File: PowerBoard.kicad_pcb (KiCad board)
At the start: 2 copper layers, 138.9 x 105.6 mm, 15 parts, among them J101 Conn_01x04_Pin, J102 Conn_01x04_Pin, J103 Conn_01x04_Pin, J104 Conn_01x04_Pin, J105 Conn_01x02_Pin, J106 Conn_01x02_Pin, J107 Conn_01x02_Pin, J108 Conn_01x06_Pin, J109 Conn_01x06_Pin, J110 USB_C_Receptacle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

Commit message: weedies
weedies
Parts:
- added G***: LOGO, memes:weedies2, F.Cu at (130.0, 82.4)
- moved U101 50.8 mm to (115.9, 129.7)
- moved J102 46.9 mm to (131.4, 52.1)
- moved J101 46.9 mm to (114.8, 52.0)
- moved J103 46.9 mm to (148.4, 52.4)
- moved J104 46.4 mm to (165.2, 52.3)
- moved J109 46.1 mm to (208.1, 48.8)
- moved J106 46.1 mm to (228.3, 48.5)
- moved J105 45.9 mm to (198.0, 48.8)
- moved J108 45.8 mm to (177.9, 48.6)
- moved J110 40.5 mm to (135.3, 134.5), turned to -90 degrees
- moved R104 38.8 mm to (186.3, 76.0)
- moved D101 38.8 mm to (186.4, 73.5)
- moved U103 38.8 mm to (187.2, 63.4)
- moved U104 38.4 mm to (144.5, 112.2)
- moved J107 36.9 mm to (172.1, 95.7)
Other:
- board size 138.9 x 105.6 mm -> 139.1 x 147.4 mm

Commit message: Big Moves
Big Moves
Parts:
- removed G***: LOGO, memes:weedies2
- U101: footprint MCU_Teensy:Teensy_4.1 -> MCU_Teensy:Teensy41_bare_pins
- moved J107 45.4 mm to (209.4, 69.8), turned to 45 degrees
- moved U104 31.5 mm to (172.2, 97.2), turned to 45 degrees
- moved J110 27.6 mm to (118.5, 156.4), turned to 45 degrees
- moved U101 20.7 mm to (114.5, 109.1)
- moved D101 11.7 mm to (183.8, 84.8), turned to 90 degrees
- moved R104 5.92 mm to (183.8, 81.3), turned to -90 degrees
- moved U103 5.52 mm to (187.3, 68.9), turned to 45 degrees
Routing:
- net 3V3: track 0.00 -> 208.3 mm, vias 0 -> 6
- net 5V: track 0.00 -> 159.8 mm, vias 0 -> 2
- net /L298N2_ENA: track 0.00 -> 150.4 mm, vias 0 -> 1
- net /L298N2_IN1: track 0.00 -> 147.2 mm, vias 0 -> 1
- net /L298N2_IN2: track 0.00 -> 142.9 mm, vias 0 -> 1
- net /L298N1_ENA: track 0.00 -> 142.6 mm, vias 0 -> 2
- net /L298N2_IN3: track 0.00 -> 138.4 mm, vias 0 -> 1
- net /L298N1_IN1: track 0.00 -> 137.9 mm, vias 0 -> 2
- net /L298N2_IN4: track 0.00 -> 133.6 mm, vias 0 -> 1
- net /L298N1_IN2: track 0.00 -> 133.1 mm, vias 0 -> 2
- net /L298N2_ENB: track 0.00 -> 129.2 mm, vias 0 -> 1
- net /L298N1_IN3: track 0.00 -> 128.2 mm, vias 0 -> 2
- net /Motor4_A: track 0.00 -> 124.6 mm, vias 0 -> 4
- net /L298N1_IN4: track 0.00 -> 124.5 mm, vias 0 -> 2
- net /Motor4_B: track 0.00 -> 124.4 mm, vias 0 -> 4
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- added copper zone on B.Cu, net GND
- added copper zone on F.Cu, net GND

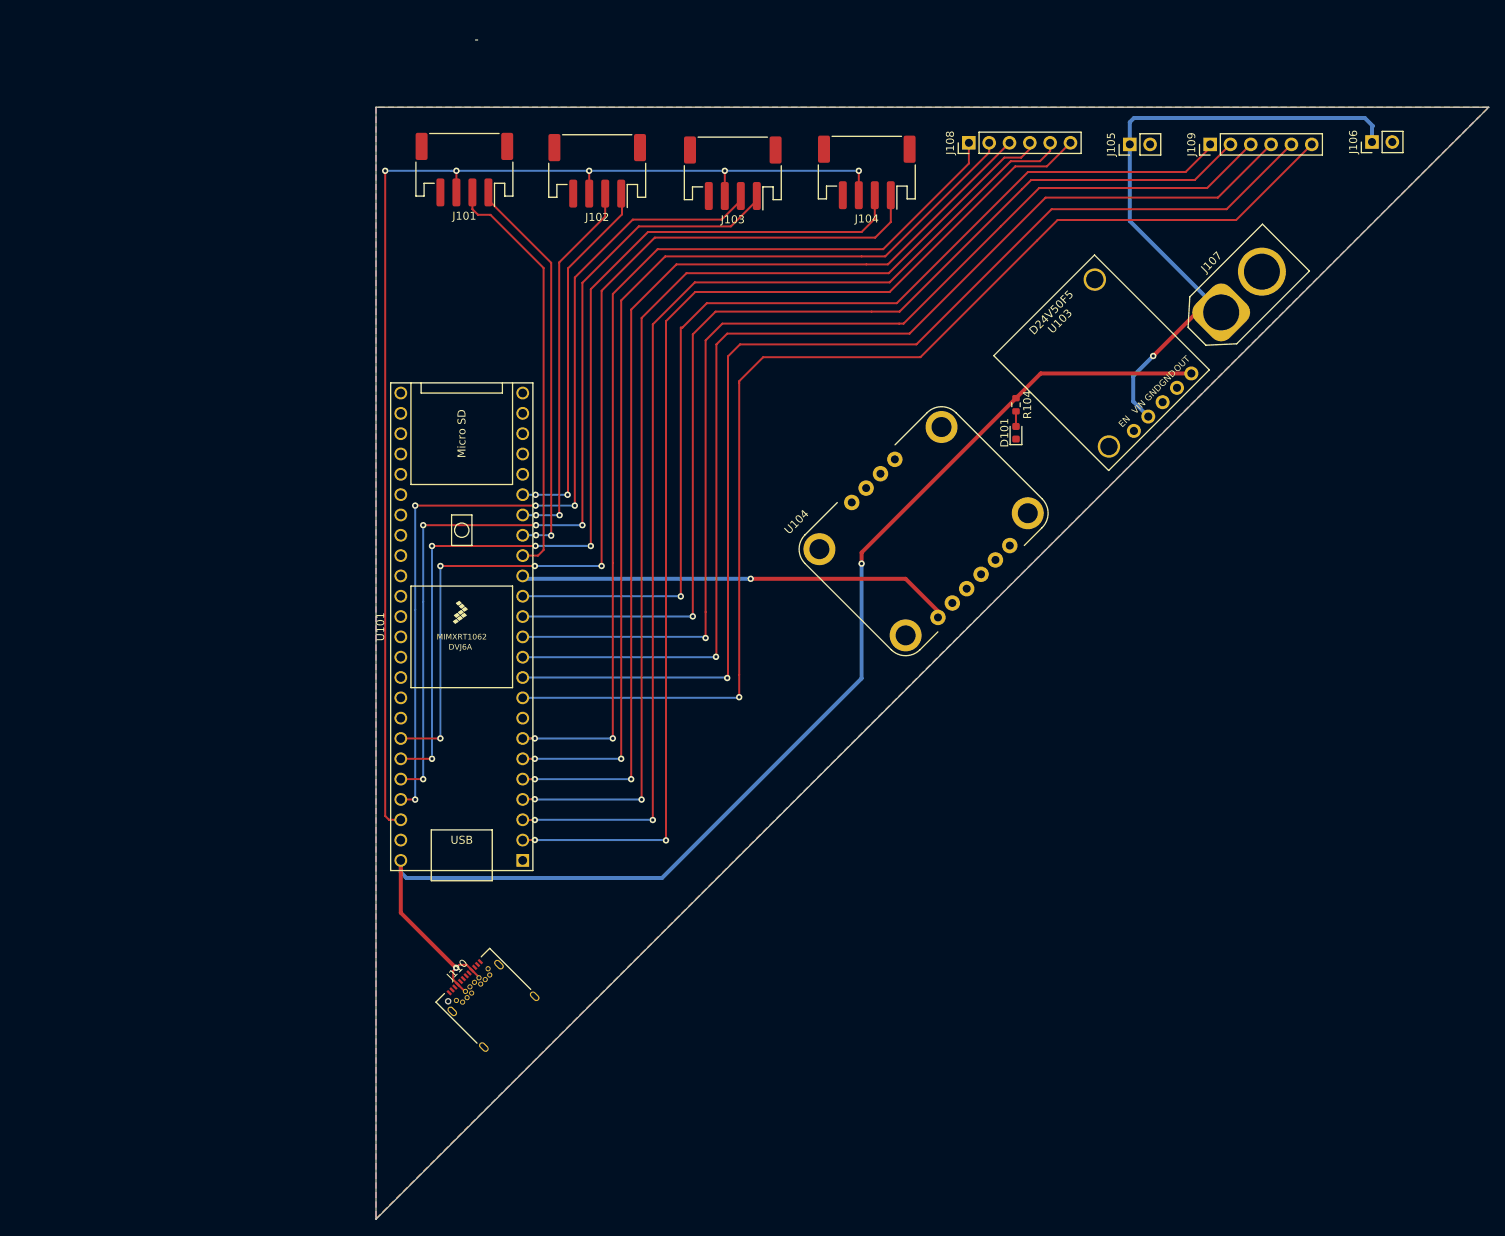
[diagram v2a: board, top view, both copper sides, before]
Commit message: some small routing touchups
made power traces much larger, made battery connector GND pad thermal reliefs larger, organized trace spacing a bit more, deleted some vias that didn't add anything, added a 15mil keepout around the board perimeter for manufacturing, and squared off the 45 degree corners for manufacturing to fix the board edge
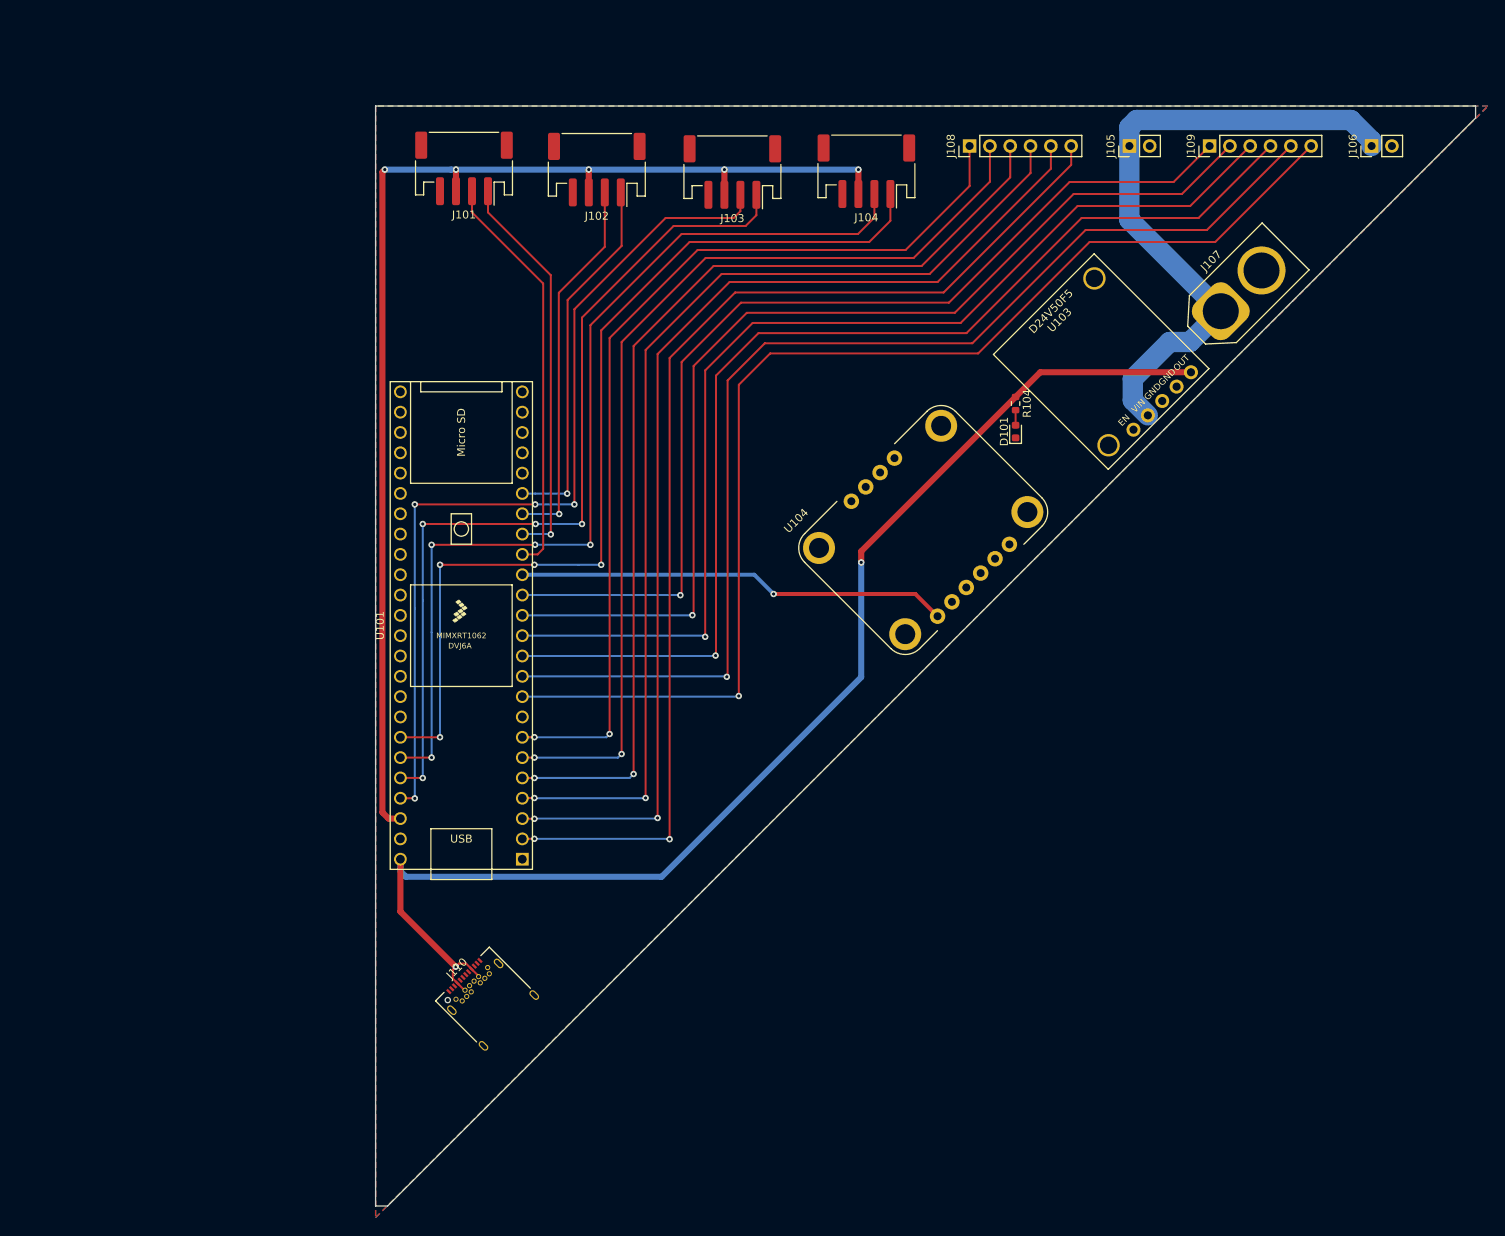
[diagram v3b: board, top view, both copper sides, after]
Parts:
- moved J106 0.50 mm to (228.2, 49.0)
- moved J108 0.41 mm to (178.0, 49.0)
- moved J109 0.21 mm to (208.0, 49.0)
- moved J105 0.21 mm to (198.0, 49.0)
- moved D101 0.16 mm to (183.7, 84.7)
- moved R104 0.16 mm to (183.7, 81.2)
- moved U103 0.16 mm to (187.3, 68.8)
- moved U104 0.16 mm to (172.2, 97.0)
- moved J101 0.16 mm to (114.8, 51.8)
- moved U101 0.16 mm to (114.5, 108.9)
- moved J103 0.16 mm to (148.3, 52.2)
- moved J104 0.16 mm to (165.1, 52.1)
- moved J102 0.16 mm to (131.4, 52.0)
- moved J107 0.16 mm to (209.4, 69.7)
- moved J110 0.16 mm to (118.4, 156.3)
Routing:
- net /L298N2_ENB: track 129.2 -> 126.2 mm
- net /Motor4_B: track 124.4 -> 121.4 mm
- net /Motor4_A: track 124.6 -> 121.8 mm
- net /L298N2_IN4: track 133.6 -> 130.9 mm
- net /L298N2_IN2: track 142.9 -> 140.4 mm
- net /L298N2_IN3: track 138.4 -> 136.0 mm
- net /L298N1_ENB: track 122.2 -> 120.0 mm
- net /L298N2_IN1: track 147.2 -> 145.2 mm
- net VIN: track 81.7 -> 80.0 mm, vias 1 -> 0
- net /L298N1_IN4: track 124.5 -> 122.9 mm
- net /Motor3_A: track 112.3 -> 110.8 mm
- net /L298N1_ENA: track 142.6 -> 141.1 mm
- net /Motor3_B: track 111.4 -> 109.9 mm
- net /L298N1_IN1: track 137.9 -> 136.6 mm
- net /L298N1_IN2: track 133.1 -> 132.1 mm
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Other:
- board size 139.1 x 147.4 mm -> 137.5 x 137.5 mm

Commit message: ready for review
Flipped encoder connector pinout, added mounting holes, fixed battery connector footprint, moved USB C connector, added memes, added placeholder names
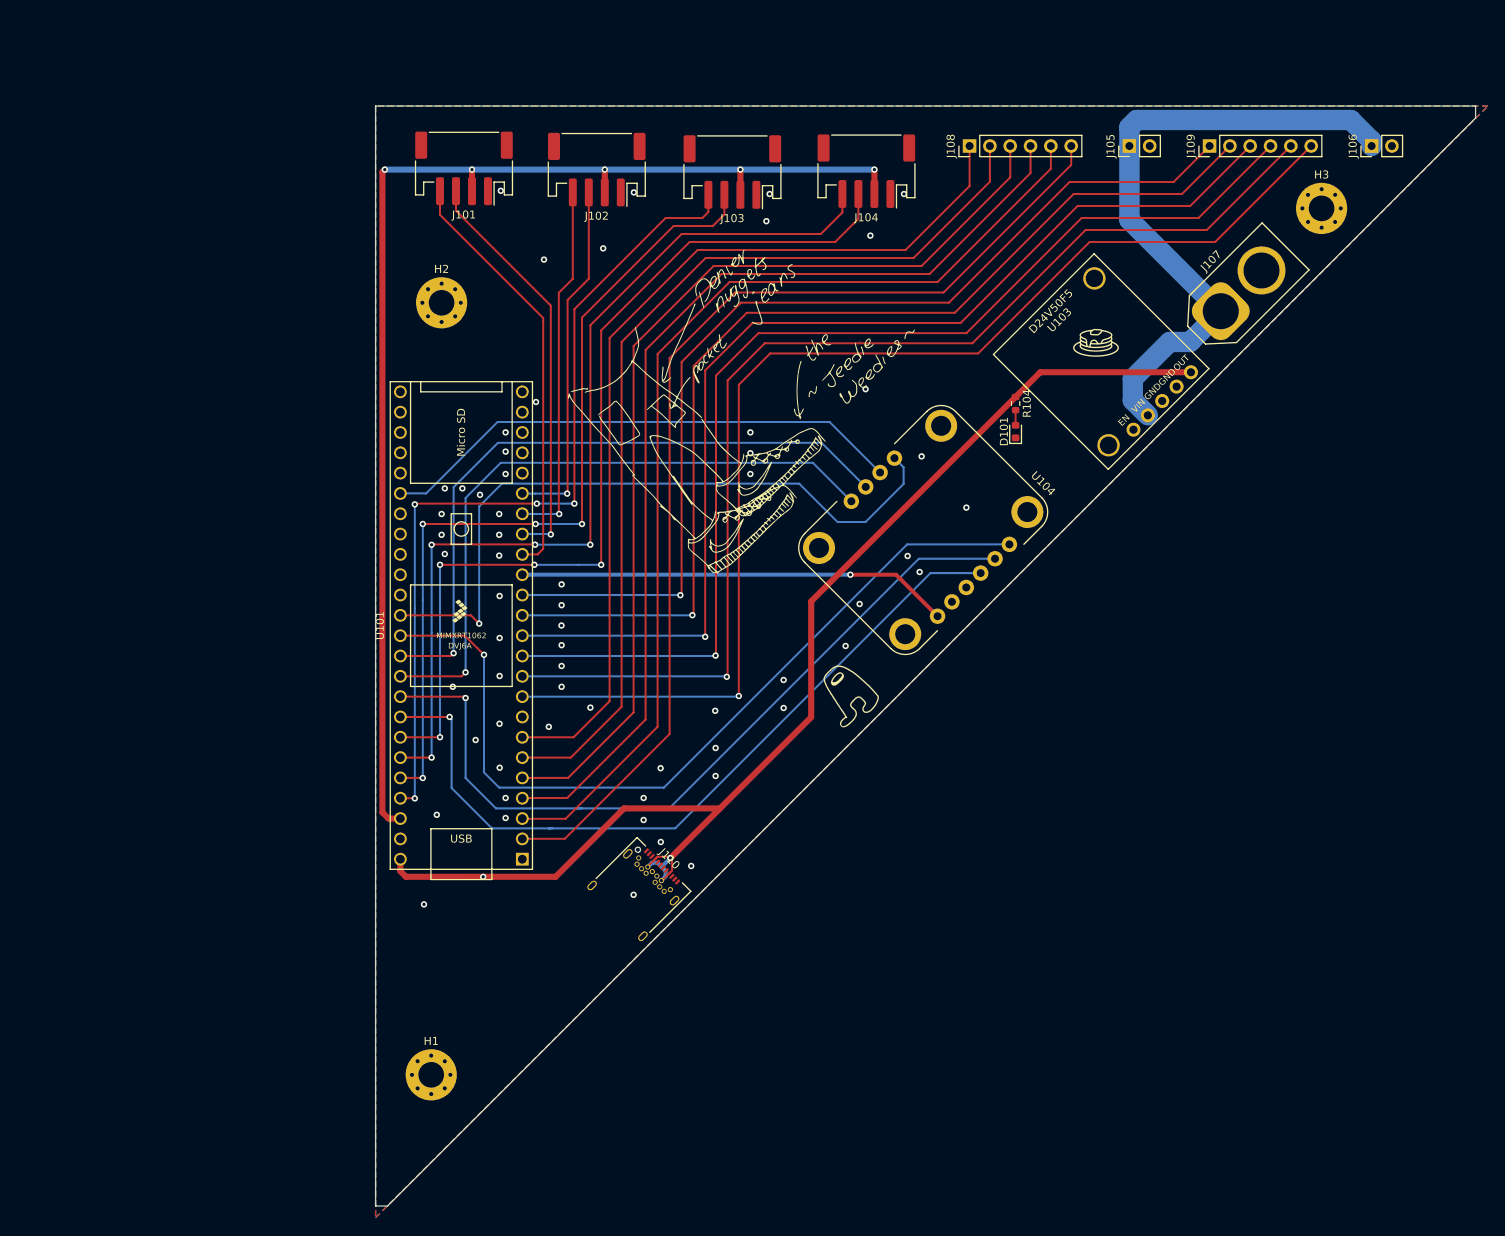
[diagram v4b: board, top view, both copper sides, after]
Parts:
- added G***: LOGO, memes:weedies2, F.Cu at (152.3, 78.0)
- added G***: LOGO, memes:pancakes, F.Cu at (193.8, 73.6)
- added G***: LOGO, memes:Amogus, F.Cu at (162.4, 117.7)
- added H1: MountingHole_Pad, MountingHole:MountingHole_3.2mm_M3_Pad_Via, F.Cu at (110.7, 165.1)
- added H2: MountingHole_Pad, MountingHole:MountingHole_3.2mm_M3_Pad_Via, F.Cu at (112.0, 68.6)
- added H3: MountingHole_Pad, MountingHole:MountingHole_3.2mm_M3_Pad_Via, F.Cu at (222.0, 56.8)
- J107: footprint Connector_AMASS:AMASS_XT60-F_1x02_P7.20mm_Vertical -> Connector_AMASS:AMASS_XT60-M_1x02_P7.20mm_Vertical
- moved J110 22.3 mm to (136.0, 142.6), turned to -45 degrees
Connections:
- J101 pad 1: /Motor1_B -> GND
- J101 pad 2: /Motor1_A -> 3V3
- J101 pad 3: 3V3 -> /Motor1_A
- J101 pad 4: GND -> /Motor1_B
- J102 pad 1: /Motor2_B -> GND
- J102 pad 2: /Motor2_A -> 3V3
- J102 pad 3: 3V3 -> /Motor2_A
- J102 pad 4: GND -> /Motor2_B
- J103 pad 1: /Motor3_B -> GND
- J103 pad 2: /Motor3_A -> 3V3
- J103 pad 3: 3V3 -> /Motor3_A
- J103 pad 4: GND -> /Motor3_B
- J104 pad 1: /Motor4_B -> GND
- J104 pad 2: /Motor4_A -> 3V3
- J104 pad 3: 3V3 -> /Motor4_A
- J104 pad 4: GND -> /Motor4_B
- U101 pad 16: /Motor1_A -> /Motor1_B
- U101 pad 17: /Motor1_B -> /Motor1_A
- U101 pad 18: /Motor2_A -> /Motor2_B
- U101 pad 19: /Motor2_B -> /Motor2_A
- U101 pad 36: unconnected-(U101-14_A0_TX3_SPDIF_OUT-Pad36) -> /IMU_ADR
- U101 pad 37: unconnected-(U101-15_A1_RX3_SPDIF_IN-Pad37) -> /IMU_RST
- U101 pad 38: unconnected-(U101-16_A2_RX4_SCL1-Pad38) -> /IMU_PS1
- U101 pad 39: unconnected-(U101-17_A3_TX4_SDA1-Pad39) -> /IMU_PS0
- U101 pad 40: unconnected-(U101-18_A4_SDA-Pad40) -> /IMU_SCL
- U101 pad 41: unconnected-(U101-19_A5_SCL-Pad41) -> /IMU_SDA
- U101 pad 42: /Motor4_B -> /Motor4_A
- U101 pad 43: /Motor4_A -> /Motor4_B
- U101 pad 44: /Motor3_B -> /Motor3_A
- U101 pad 45: /Motor3_A -> /Motor3_B
- U104 pad 10: unconnected-(U104-PS0-Pad10) -> /IMU_PS0
- U104 pad 4: unconnected-(U104-SDA-Pad4) -> /IMU_SDA
- U104 pad 5: unconnected-(U104-SCL-Pad5) -> /IMU_SCL
- U104 pad 6: unconnected-(U104-RST-Pad6) -> /IMU_RST
- U104 pad 7: unconnected-(U104-ADR-Pad7) -> /IMU_ADR
- U104 pad 9: unconnected-(U104-PS1-Pad9) -> /IMU_PS1
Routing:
- net /IMU_RST: track 0.00 -> 105.2 mm, vias 0 -> 1
- net /IMU_SCL: track 0.00 -> 99.7 mm, vias 0 -> 1
- net /IMU_SDA: track 0.00 -> 97.1 mm, vias 0 -> 1
- net /IMU_ADR: track 0.00 -> 86.8 mm, vias 0 -> 1
- net /IMU_PS1: track 0.00 -> 83.6 mm, vias 0 -> 1
- net /IMU_PS0: track 0.00 -> 82.2 mm, vias 0 -> 1
- net /BNO_INT: track 0.00 -> 66.3 mm
- net /L298N1_ENA: track 141.1 -> 133.4 mm, vias 2 -> 0
- net /L298N1_IN1: track 136.6 -> 129.9 mm, vias 2 -> 0
- net /L298N1_IN2: track 132.1 -> 126.3 mm, vias 2 -> 0
- net /Motor3_A: track 110.8 -> 105.8 mm
- net /Motor4_A: track 121.8 -> 117.2 mm
- net /L298N1_IN3: track 127.4 -> 122.8 mm, vias 2 -> 0
- net /Motor4_B: track 121.4 -> 117.5 mm
- net /L298N1_ENB: track 120.0 -> 116.1 mm, vias 2 -> 0
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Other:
- board text added: "Dr. Mr. R. Bhog Alex Alex Rishi Gautam Other Names Placeholder Placeholder Placeholder so many people who worked on this project it's great so awesome let's go more names placeholder"

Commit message: only need names
should be ready to order the board once we get list of names for back silkscreen
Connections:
- U101 pad 40: /IMU_SCL -> /IMU_SDA
- U101 pad 41: /IMU_SDA -> /IMU_SCL
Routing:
- net 3V3: track 210.0 -> 248.8 mm
- net /IMU_SCL: track 99.7 -> 97.1 mm
- net /IMU_SDA: track 97.1 -> 99.6 mm
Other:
- board text added: "3V3"
- board text added: "A"
- board text added: "B"
- board text added: "ENA"
- board text added: "ENB"
- board text added: "GND"
- board text added: "IN1"
- board text added: "IN2"
- board text added: "IN3"
- board text added: "IN4"
- board text added: "VBAT"

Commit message: ready to order
added more memes and updated name list
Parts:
- added G***: LOGO, memes:300parasangstall_teensy, F.Cu at (131.6, 109.2)
- added G***: LOGO, memes:enumclaw_70mm, B.Cu at (172.4, 74.4)
- moved G*** 9.66 mm to (160.4, 72.8)
- moved J110 5.17 mm to (132.2, 146.1)
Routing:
- net 5V: track 156.8 -> 162.0 mm
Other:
- board text added: "2x Alex Bizzy Bone Rishi Gautam Gautam Surag (Gautam) Gautam Ary Gautam Sid Gautam Magilan Gautam Gautam Evan Eungi"
- board text added: "Dr. Mr. R Bhog"
- board text added: "The Purple Homie"
- board text removed: "Dr. Mr. R. Bhog Alex Alex Rishi Gautam Other Names Placeholder Placeholder Placeholder so many people who worked on this project it's great so awesome let's go more names placeholder"
